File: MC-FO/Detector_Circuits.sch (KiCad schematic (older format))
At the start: 9 parts, among them U141 IFD97, U142 TLV3501AID, U143 74LVC1G32SE-7

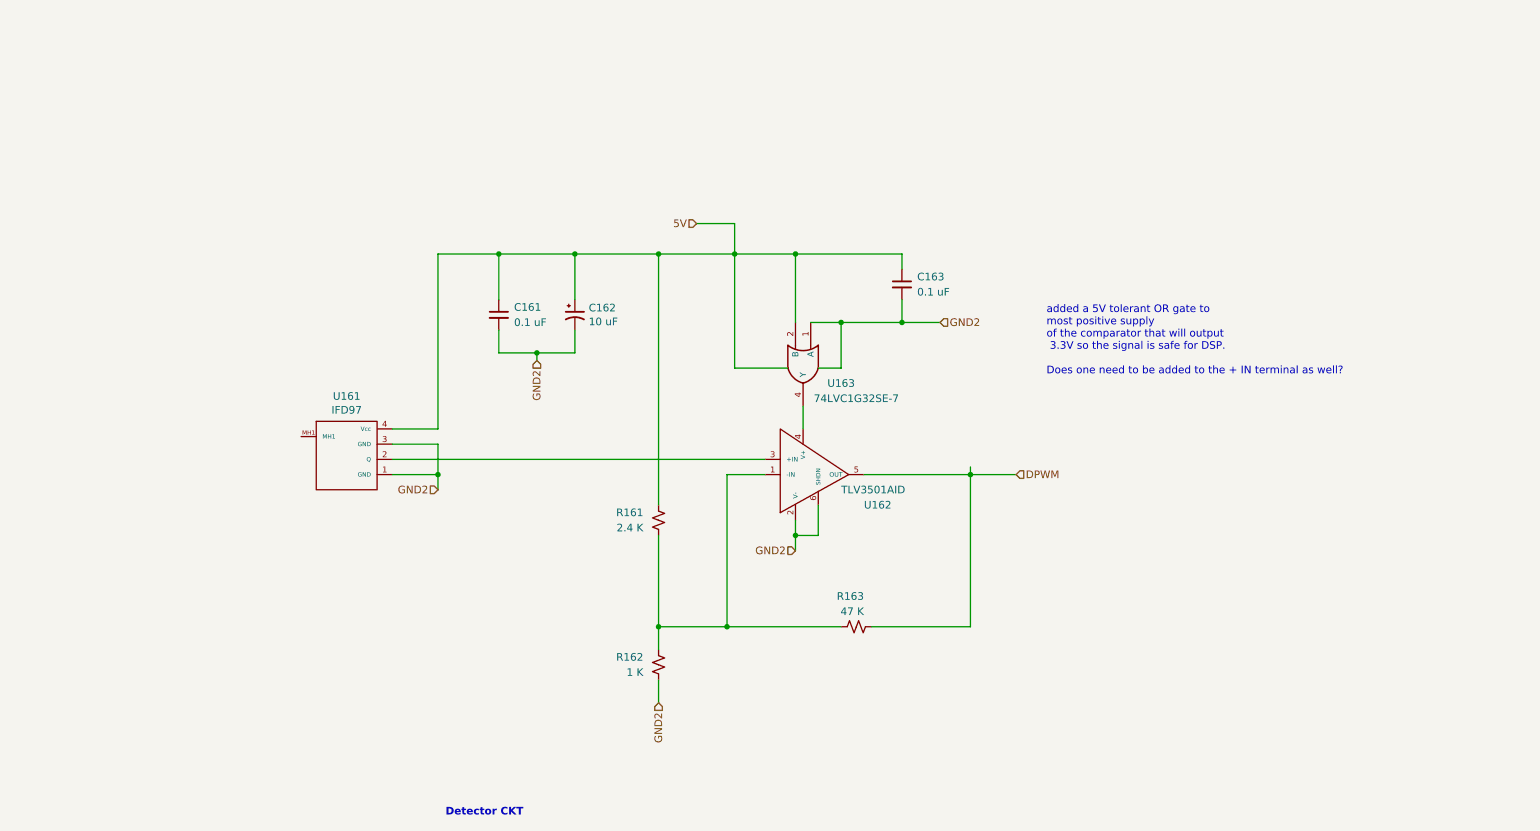
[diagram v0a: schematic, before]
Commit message: Fixed file hierarchy
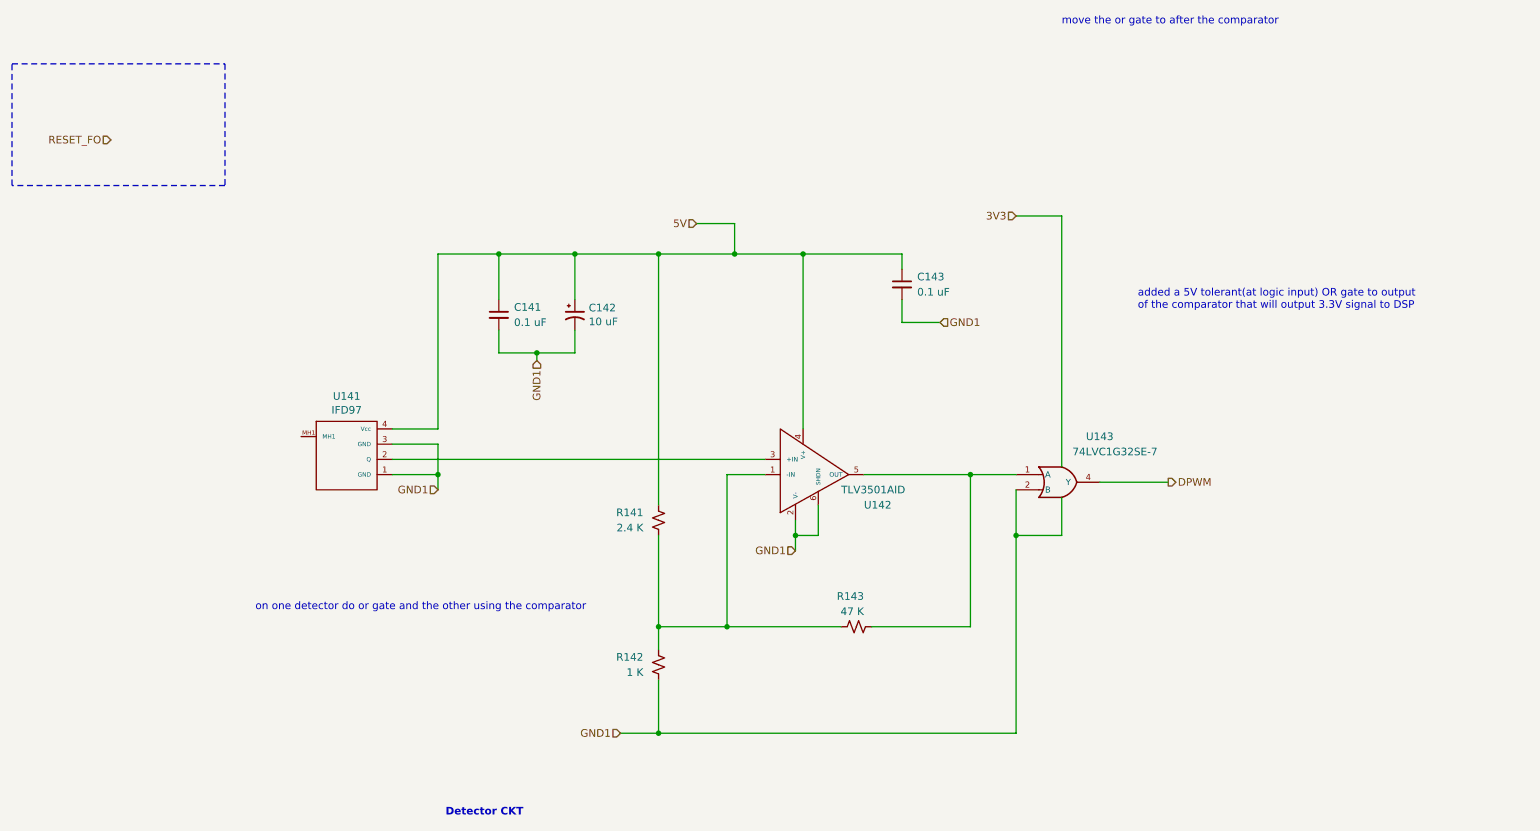
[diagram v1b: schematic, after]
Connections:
- net DPWM: now also U143.4 (Y); no longer R143.2, U142.5 (OUT)
- net GND: now also C141.2, C142.2, C143.2, R142.1, U141.1 (GND), U141.3 (GND), U142.2 (V-), U142.6 (SHDN); no longer C141.1, C142.1, C143.1, R141.2, U141.4 (Vcc)
- net VCC: no longer C141.2, C142.2, C143.2, R142.1, U141.1 (GND), U141.3 (GND), U142.2 (V-), U142.6 (SHDN), U143.1 (A)
- net 5V: now reaches U142.4 (V+)
- net 5V: now also C141.1, C142.1, C143.1, R141.2, U141.4 (Vcc); no longer U143.4 (Y)
- new net: R143.2, U142.5 (OUT), U143.1 (A)
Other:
- note added: "added a 5V tolerant(at logic input) OR gate to output\nof the comparator that will output 3.3V signal to DSP\n\n"
- note added: "move the or gate to after the comparator"
- note added: "on one detector do or gate and the other using the comparator"
- note removed: "added a 5V tolerant OR gate to \nmost positive supply\nof the comparator that will output\n 3.3V so the signal is safe for DSP.\n\nDoes one need to be added to the + IN terminal as well?"
- moved on the sheet: U143
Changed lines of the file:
@@
 AR Path="/6171C819/6178E7F5" Ref="C143"  Part="1"
 AR Path="/61724A08/6178E7F5" Ref="C163"  Part="1"
-F 0 "C163" H 7450 2450 50  0000 L CNN
+F 0 "C143" H 7450 2450 50  0000 L CNN
 F 1 "0.1 uF" H 7450 2350 50  0000 L CNN
 F 2 "Capacitor_SMD:C_0603_1608Metric" H 7350 2400 50  0001 C CNN
@@
 AR Path="/6171C819/6178E7F6" Ref="C141"  Part="1"
 AR Path="/61724A08/6178E7F6" Ref="C161"  Part="1"
-F 0 "C161" H 4800 2650 50  0000 L CNN
+F 0 "C141" H 4800 2650 50  0000 L CNN
 F 1 "0.1 uF" H 4800 2550 50  0000 L CNN
 F 2 "Capacitor_SMD:C_0603_1608Metric" H 4700 2600 50  0001 C CNN
@@
 AR Path="/6171C819/6174EB5A" Ref="R141"  Part="1"
 AR Path="/61724A08/6174EB5A" Ref="R161"  Part="1"
-F 0 "R161" H 5850 3900 50  0000 L CNN
+F 0 "R141" H 5850 3900 50  0000 L CNN
 F 1 "2.4 K" H 5850 4000 50  0000 L CNN
 F 2 "Resistor_SMD:R_0603_1608Metric" H 5750 3950 50  0001 C CNN
@@
 AR Path="/6171C819/61720E6A" Ref="C142"  Part="1"
 AR Path="/61724A08/61720E6A" Ref="C162"  Part="1"
-F 0 "C162" H 5291 2646 50  0000 L CNN
+F 0 "C142" H 5291 2646 50  0000 L CNN
 F 1 "10 uF" H 5291 2555 50  0000 L CNN
 F 2 "Capacitor_SMD:C_0603_1608Metric" H 5200 2600 50  0001 C CNN
@@
 AR Path="/6171C819/617451F8" Ref="R142"  Part="1"
 AR Path="/61724A08/617451F8" Ref="R162"  Part="1"
-F 0 "R162" H 5850 4850 50  0000 L CNN
+F 0 "R142" H 5850 4850 50  0000 L CNN
 F 1 "1 K" H 5850 4950 50  0000 L CNN
 F 2 "Resistor_SMD:R_0603_1608Metric" H 5750 4900 50  0001 C CNN
@@
 AR Path="/6171C819/61745A42" Ref="R143"  Part="1"
 AR Path="/61724A08/61745A42" Ref="R163"  Part="1"
-F 0 "R163" V 7250 4600 50  0000 L CNN
+F 0 "R143" V 7250 4600 50  0000 L CNN
 F 1 "47 K" V 7150 4600 50  0000 L CNN
 F 2 "Resistor_SMD:R_0603_1608Metric" H 7050 4650 50  0001 C CNN
@@
 $EndComp
 Wire Wire Line
-	5750 5150 5750 5000
-Wire Wire Line
 	5750 4800 5750 4650
 Wire Wire Line
@@
 	6250 2000 6250 2200
 Connection ~ 6250 2200
-Wire Wire Line
-	6700 3350 6700 3200
 Connection ~ 6200 4650
 Wire Wire Line
@@
 AR Path="/6171C819/61758365" Ref="U141"  Part="1"
 AR Path="/61724A08/61758365" Ref="U161"  Part="1"
-F 0 "U161" H 3700 4765 50  0000 C CNN
+F 0 "U141" H 3700 4765 50  0000 C CNN
 F 1 "IFD97" H 3700 4674 50  0000 C CNN
 F 2 "Footprints_MC-FO:IFD97" H 3700 4750 50  0001 C CNN
@@
 	1    0    0    -1
 $EndComp
-Text HLabel 8100 3650 2    50   Input ~ 0
+Text HLabel 9100 3700 2    50   Output ~ 0
 DPWM
 Text HLabel 6000 2000 0    50   Input ~ 0
@@
 AR Path="/6171C819/61744BAA" Ref="U142"  Part="1"
 AR Path="/61724A08/61744BAA" Ref="U162"  Part="1"
-F 0 "U162" H 7100 3850 50  0000 L CNN
+F 0 "U142" H 7100 3850 50  0000 L CNN
 F 1 "TLV3501AID" H 6950 3750 50  0000 L CNN
 F 2 "Package_SO:SOIC-8_3.9x4.9mm_P1.27mm" H 6600 3950 50  0001 C CNN
@@
 Connection ~ 6650 4050
 Connection ~ 7800 3650
-Wire Wire Line
-	7800 3650 7800 3600
-Text HLabel 5750 5150 3    50   Input ~ 0
-GND2
+Text HLabel 5500 5350 0    50   Input ~ 0
+GND1
 Text HLabel 6650 4150 0    50   Input ~ 0
-GND2
+GND1
 Text HLabel 4950 2900 3    50   Input ~ 0
-GND2
+GND1
 Text HLabel 4300 3750 0    50   Input ~ 0
-GND2
+GND1
 Text HLabel 7600 2650 2    50   Input ~ 0
-GND2
-Text Notes 8300 3000 0    50   ~ 0
-added a 5V tolerant OR gate to \nmost positive supply\nof the comparator that will output\n 3.3V so the signal is safe for DSP.\n\nDoes one need to be added to the + IN terminal as well?
+GND1
 Wire Wire Line
 	4700 2850 4950 2850
@@
 Wire Wire Line
 	4950 2850 5200 2850
+Wire Wire Line
+	7350 2500 7350 2650
+Wire Wire Line
+	7350 2200 7350 2300
+Wire Wire Line
+	7350 2650 7600 2650
+Wire Wire Line
+	5750 2200 5750 3850
+Wire Wire Line
+	4000 3550 6450 3550
+Text Notes 8400 700  0    50   ~ 0
+move the or gate to after the comparator
+Text Notes 3100 4550 0    50   ~ 0
+on one detector do or gate and the other using the comparator
+Wire Notes Line
+	1500 950  2900 950
+Wire Notes Line
+	2900 950  2900 1750
+Wire Notes Line
+	2900 1750 1500 1750
+Wire Notes Line
+	1500 1750 1500 950
+Text HLabel 2150 1450 0    50   Input ~ 0
+RESET_FO
+Wire Wire Line
+	8650 3700 9100 3700
 $Comp
 L Existing_IC_Models:74LVC1G32SE-7 U143
 U 1 1 617F3635
-P 6700 2950
+P 8400 3700
 AR Path="/6171C819/617F3635" Ref="U143"  Part="1"
 AR Path="/61724A08/617F3635" Ref="U163"  Part="1"
-F 0 "U163" V 6800 3200 50  0000 C CNN
-F 1 "74LVC1G32SE-7" V 6900 3300 50  0000 C CNN
-F 2 "Package_TO_SOT_SMD:SOT-353_SC-70-5" H 6700 2950 50  0001 C CNN
-F 3 "http://www.ti.com/lit/sg/scyt129e/scyt129e.pdf" H 6700 2950 50  0001 C CNN
-	1    6700 2950
-	0    1    1    0
-$EndComp
-Wire Wire Line
-	6250 2200 6650 2200
-Wire Wire Line
-	6650 2200 6650 2650
-Connection ~ 6650 2200
-Wire Wire Line
-	6650 2200 7350 2200
-Wire Wire Line
-	6600 2950 6250 2950
-Wire Wire Line
-	6250 2950 6250 2200
-Wire Wire Line
-	6750 2650 6950 2650
-Wire Wire Line
-	6800 2950 6950 2950
-Wire Wire Line
-	6950 2950 6950 2650
-Connection ~ 6950 2650
-Wire Wire Line
-	6950 2650 7350 2650
-Wire Wire Line
-	7350 2500 7350 2650
-Wire Wire Line
-	7350 2200 7350 2300
-Wire Wire Line
-	7350 2650 7600 2650
-Connection ~ 7350 2650
-Wire Wire Line
-	5750 2200 5750 3850
-Wire Wire Line
-	4000 3550 6450 3550
+F 0 "U143" H 8650 4000 50  0000 C CNN
+F 1 "74LVC1G32SE-7" H 8750 3900 50  0000 C CNN
+F 2 "Package_TO_SOT_SMD:SOT-353_SC-70-5" H 8400 3700 50  0001 C CNN
+F 3 "http://www.ti.com/lit/sg/scyt129e/scyt129e.pdf" H 8400 3700 50  0001 C CNN
+	1    8400 3700
+	1    0    0    -1
+$EndComp
+Wire Wire Line
+	6250 2200 6700 2200
+Wire Wire Line
+	6700 2200 6700 3350
+Connection ~ 6700 2200
+Wire Wire Line
+	6700 2200 7350 2200
+Wire Wire Line
+	5750 5000 5750 5350
+Wire Wire Line
+	5500 5350 5750 5350
+Wire Wire Line
+	8100 3750 8100 4050
+Wire Wire Line
+	8100 5350 5750 5350
+Connection ~ 5750 5350
+Wire Wire Line
+	8400 3600 8400 1950
+Text HLabel 8100 1950 0    50   Input ~ 0
+3V3
+Wire Wire Line
+	8100 1950 8400 1950
+Wire Wire Line
+	8400 3800 8400 4050
+Wire Wire Line
+	8400 4050 8100 4050
+Connection ~ 8100 4050
+Wire Wire Line
+	8100 4050 8100 5350
+Text Notes 8900 2650 0    50   ~ 0
+added a 5V tolerant(at logic input) OR gate to output\nof the comparator that will output 3.3V signal to DSP\n\n
 $EndSCHEMATC

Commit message: Detector2 update, RESET integration
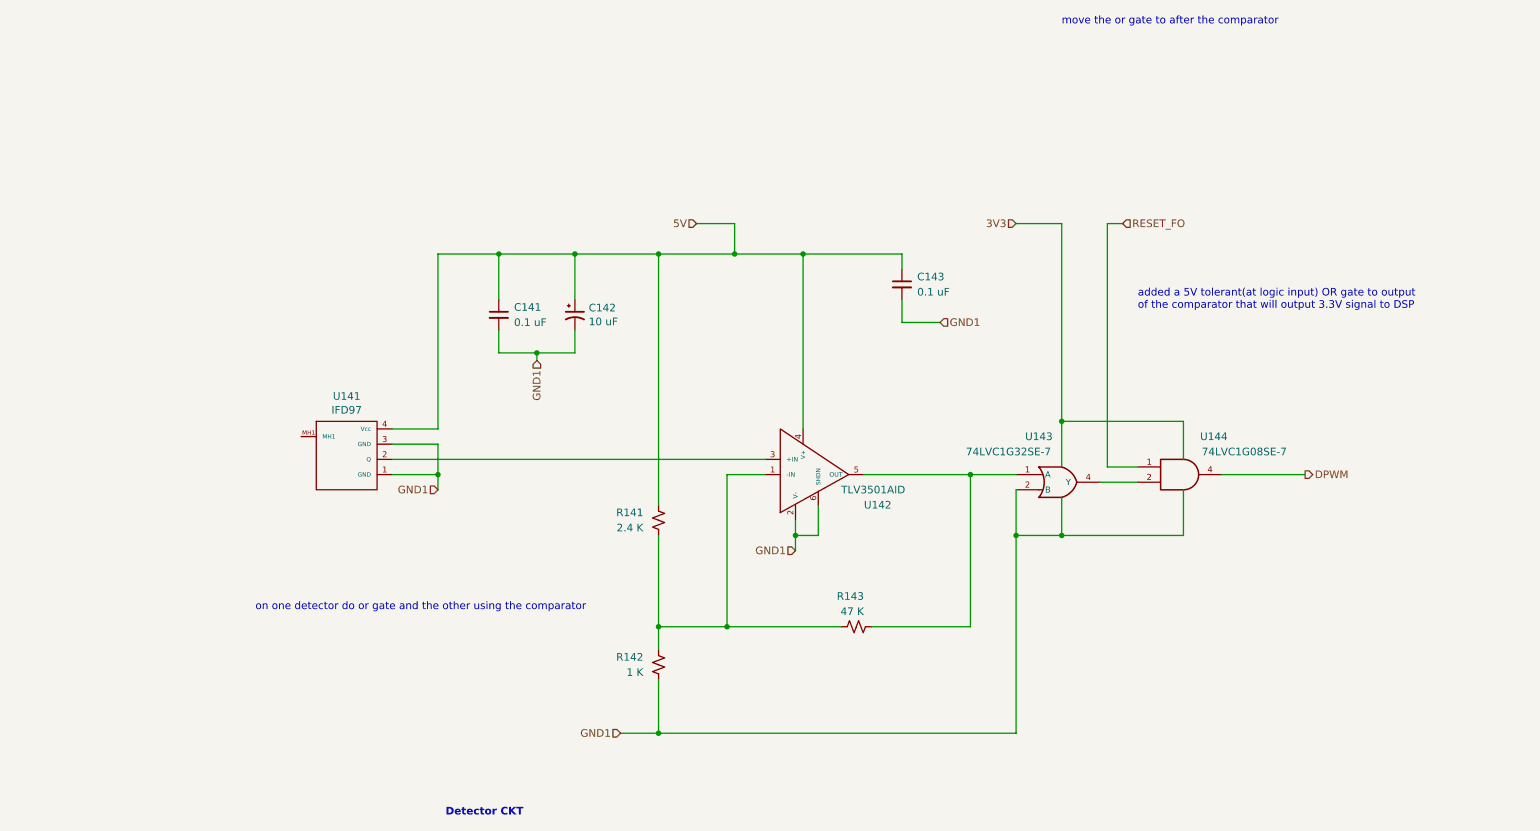
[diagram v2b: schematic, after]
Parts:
- added U144: 74LVC1G08SE-7, Package_TO_SOT_SMD:SOT-353_SC-70-5, symbol Existing_IC_Models:74LVC1G08SE-7
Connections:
- net DPWM: now also U144.4; no longer U143.4 (Y)
- net GND: now also U144.3 (GND)
- net RESET_FO: now also U144.1
- net VCC: now also U144.5 (VCC)
- new net: U143.4 (Y), U144.2
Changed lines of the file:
@@
 $Descr A4 11693 8268
 encoding utf-8
-Sheet 8 11
+Sheet 7 10
 Title ""
 Date ""
@@
 	1    0    0    -1
 $EndComp
-Text HLabel 9100 3700 2    50   Output ~ 0
+Text HLabel 10000 3650 2    50   Output ~ 0
 DPWM
 Text HLabel 6000 2000 0    50   Input ~ 0
@@
 Text Notes 3100 4550 0    50   ~ 0
 on one detector do or gate and the other using the comparator
-Wire Notes Line
-	1500 950  2900 950
-Wire Notes Line
-	2900 950  2900 1750
-Wire Notes Line
-	2900 1750 1500 1750
-Wire Notes Line
-	1500 1750 1500 950
-Text HLabel 2150 1450 0    50   Input ~ 0
+Text HLabel 8800 2000 2    50   Input ~ 0
 RESET_FO
-Wire Wire Line
-	8650 3700 9100 3700
 $Comp
 L Existing_IC_Models:74LVC1G32SE-7 U143
@@
 AR Path="/6171C819/617F3635" Ref="U143"  Part="1"
 AR Path="/61724A08/617F3635" Ref="U163"  Part="1"
-F 0 "U143" H 8650 4000 50  0000 C CNN
-F 1 "74LVC1G32SE-7" H 8750 3900 50  0000 C CNN
+F 0 "U143" H 8250 4000 50  0000 C CNN
+F 1 "74LVC1G32SE-7" H 8050 3900 50  0000 C CNN
 F 2 "Package_TO_SOT_SMD:SOT-353_SC-70-5" H 8400 3700 50  0001 C CNN
 F 3 "http://www.ti.com/lit/sg/scyt129e/scyt129e.pdf" H 8400 3700 50  0001 C CNN
@@
 Connection ~ 5750 5350
 Wire Wire Line
-	8400 3600 8400 1950
-Text HLabel 8100 1950 0    50   Input ~ 0
+	8400 3600 8400 3300
+Text HLabel 8100 2000 0    50   Input ~ 0
 3V3
 Wire Wire Line
-	8100 1950 8400 1950
+	8100 2000 8400 2000
 Wire Wire Line
 	8400 3800 8400 4050
@@
 Text Notes 8900 2650 0    50   ~ 0
 added a 5V tolerant(at logic input) OR gate to output\nof the comparator that will output 3.3V signal to DSP\n\n
+$Comp
+L Existing_IC_Models:74LVC1G08SE-7 U144
+U 1 1 61B8527D
+P 9200 3650
+F 0 "U144" H 9400 3900 50  0000 C CNN
+F 1 "74LVC1G08SE-7" H 9600 3800 50  0000 C CNN
+F 2 "Package_TO_SOT_SMD:SOT-353_SC-70-5" H 9200 3650 50  0001 C CNN
+F 3 "http://www.ti.com/lit/sg/scyt129e/scyt129e.pdf" H 9200 3650 50  0001 C CNN
+	1    9200 3650
+	1    0    0    -1
+$EndComp
+Wire Wire Line
+	8800 2000 8700 2000
+Wire Wire Line
+	8700 2000 8700 3600
+Wire Wire Line
+	8700 3600 8900 3600
+Wire Wire Line
+	8900 3700 8650 3700
+Wire Wire Line
+	8400 3300 9200 3300
+Wire Wire Line
+	9200 3300 9200 3550
+Connection ~ 8400 3300
+Wire Wire Line
+	8400 3300 8400 2000
+Wire Wire Line
+	9200 3750 9200 4050
+Wire Wire Line
+	9200 4050 8400 4050
+Connection ~ 8400 4050
+Wire Wire Line
+	9450 3650 10000 3650
 $EndSCHEMATC

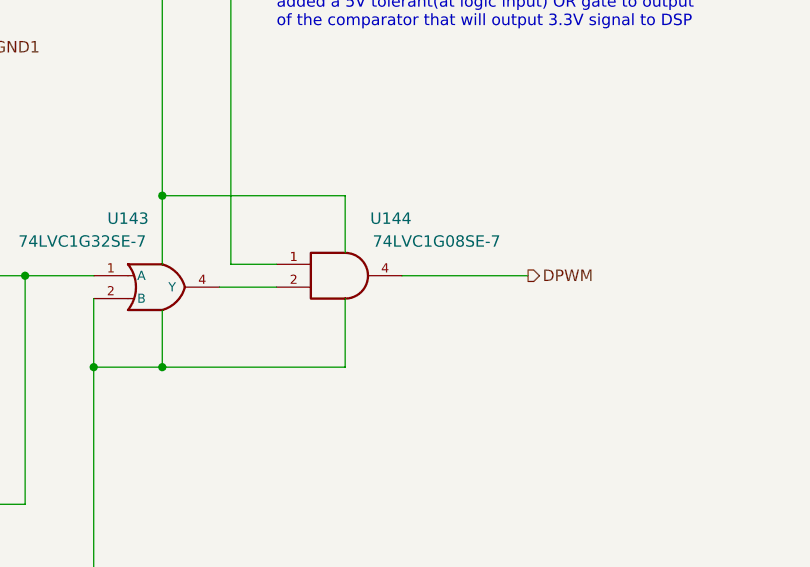
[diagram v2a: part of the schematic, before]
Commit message: add connector, reset implementation
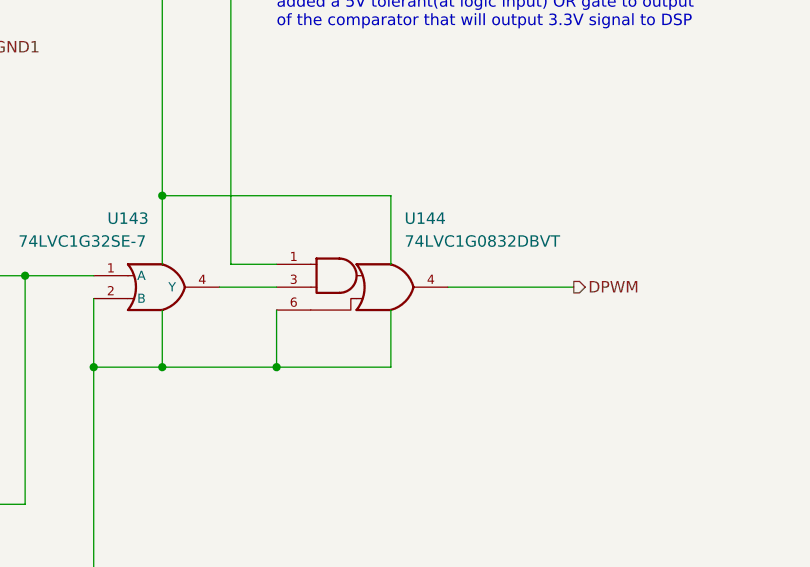
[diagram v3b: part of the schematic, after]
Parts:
- removed U144: 74LVC1G08SE-7, Package_TO_SOT_SMD:SOT-353_SC-70-5, symbol Existing_IC_Models:74LVC1G08SE-7
- added U144: 74LVC1G0832DBVT, symbol Existing_IC_Models:74LVC1G0832DBVT
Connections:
- net DPWM: now also U144.4
- net GND: now also U144.2 (GND), U144.6
- net RESET_FO: now also U144.1
- net VCC: now also U144.5 (VCC)
- net at U143.4 (Y): now also U144.3
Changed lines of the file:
@@
 	1    0    0    -1
 $EndComp
-Text HLabel 10000 3650 2    50   Output ~ 0
+Text HLabel 10200 3700 2    50   Output ~ 0
 DPWM
 Text HLabel 6000 2000 0    50   Input ~ 0
@@
 Text Notes 8900 2650 0    50   ~ 0
 added a 5V tolerant(at logic input) OR gate to output\nof the comparator that will output 3.3V signal to DSP\n\n
-$Comp
-L Existing_IC_Models:74LVC1G08SE-7 U144
-U 1 1 61B8527D
-P 9200 3650
-F 0 "U144" H 9400 3900 50  0000 C CNN
-F 1 "74LVC1G08SE-7" H 9600 3800 50  0000 C CNN
-F 2 "Package_TO_SOT_SMD:SOT-353_SC-70-5" H 9200 3650 50  0001 C CNN
-F 3 "http://www.ti.com/lit/sg/scyt129e/scyt129e.pdf" H 9200 3650 50  0001 C CNN
-	1    9200 3650
-	1    0    0    -1
-$EndComp
 Wire Wire Line
 	8800 2000 8700 2000
@@
 Wire Wire Line
 	8900 3700 8650 3700
-Wire Wire Line
-	8400 3300 9200 3300
-Wire Wire Line
-	9200 3300 9200 3550
 Connection ~ 8400 3300
 Wire Wire Line
 	8400 3300 8400 2000
 Wire Wire Line
-	9200 3750 9200 4050
-Wire Wire Line
-	9200 4050 8400 4050
+	9650 3700 10200 3700
+$Comp
+L Existing_IC_Models:74LVC1G0832DBVT U144
+U 1 1 618B7235
+P 9250 3700
+F 0 "U144" H 9550 4000 50  0000 C CNN
+F 1 "74LVC1G0832DBVT" H 9800 3900 50  0000 C CNN
+F 2 "" H 9250 3700 50  0001 C CNN
+F 3 "http://www.ti.com/lit/sg/scyt129e/scyt129e.pdf" H 9250 3700 50  0001 C CNN
+	1    9250 3700
+	1    0    0    -1
+$EndComp
 Connection ~ 8400 4050
 Wire Wire Line
-	9450 3650 10000 3650
+	9400 3300 9400 3600
+Wire Wire Line
+	8400 3300 9400 3300
+Wire Wire Line
+	8900 4050 8900 3800
+Wire Wire Line
+	8400 4050 8900 4050
+Wire Wire Line
+	8900 4050 9400 4050
+Wire Wire Line
+	9400 4050 9400 3800
+Connection ~ 8900 4050
 $EndSCHEMATC

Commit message: update footprints, resistors
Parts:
- U141: footprint Footprints_MC-FO:IFD97 -> Footprints_MC-FO:IFE98
- U144: footprint (none) -> Package_TO_SOT_SMD:SOT-23-6
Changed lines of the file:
@@
 F 0 "U141" H 3700 4765 50  0000 C CNN
 F 1 "IFD97" H 3700 4674 50  0000 C CNN
-F 2 "Footprints_MC-FO:IFD97" H 3700 4750 50  0001 C CNN
+F 2 "Footprints_MC-FO:IFE98" H 3700 4750 50  0001 C CNN
 F 3 "" H 3700 4750 50  0001 C CNN
 	1    3700 3950
@@
 F 0 "U144" H 9550 4000 50  0000 C CNN
 F 1 "74LVC1G0832DBVT" H 9800 3900 50  0000 C CNN
-F 2 "" H 9250 3700 50  0001 C CNN
+F 2 "Package_TO_SOT_SMD:SOT-23-6" H 9250 3700 50  0001 C CNN
 F 3 "http://www.ti.com/lit/sg/scyt129e/scyt129e.pdf" H 9250 3700 50  0001 C CNN
 	1    9250 3700
